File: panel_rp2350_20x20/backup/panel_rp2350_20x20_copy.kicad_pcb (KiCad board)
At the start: 6 copper layers, 45 x 45 mm, 548 parts, among them J1 Conn_01x04, J2 Conn_01x05, J3 Conn_01x05, J4 Conn_01x05, J5 Conn_01x05, SW1 SW_Push, SW2 SW_Push, U1 APS6404L-3SQR, U10 UCC27517, U11 UCC27517, U12 UCC27517, U13 UCC27517, U14 UCC27517, U15 UCC27517, U16 UCC27517, U17 UCC27517, U18 UCC27517, U19 UCC27517, U2 RP2354B_80QFN, U20 UCC27517, U21 UCC27517, U22 UCC27517, U23 UCC27517, U24 UCC27517, U25 UCC27517, U26 UCC27517, U27 UCC27517, U28 UCC27517, U29 UCC27517, U3 UCC27517, U30 UCC27517, U31 UCC27517, U32 UCC27517, U33 UCC27517, U34 UCC27517, U35 UCC27517, U36 UCC27517, U37 UCC27517, U38 UCC27517, U39 UCC27517, U4 UCC27517, U40 UCC27517, U41 UCC27517, U42 UCC27517, U43 AP2112K-3.3, U5 UCC27517, U6 UCC27517, U7 UCC27517, U8 UCC27517, U9 UCC27517, Y1 ABM8-272-T3

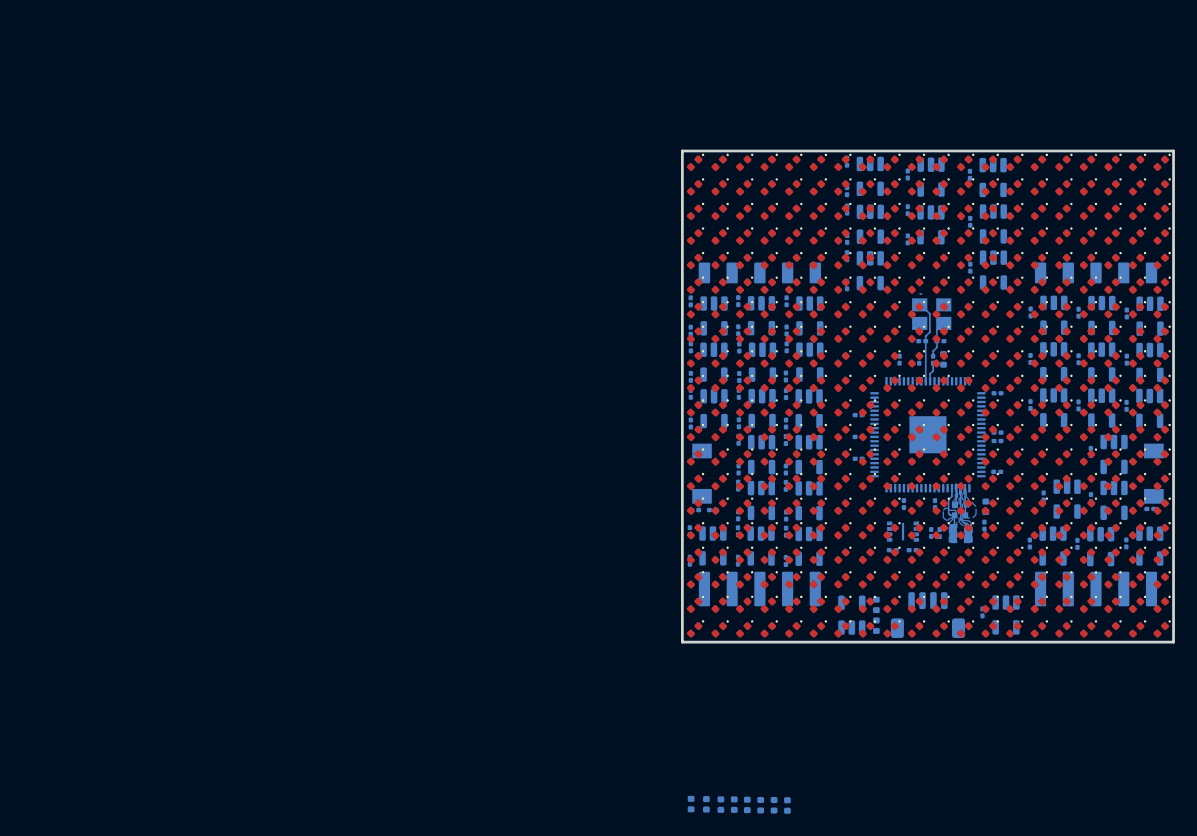
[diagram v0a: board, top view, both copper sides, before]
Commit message: More work on rp2350 20x20 panel.
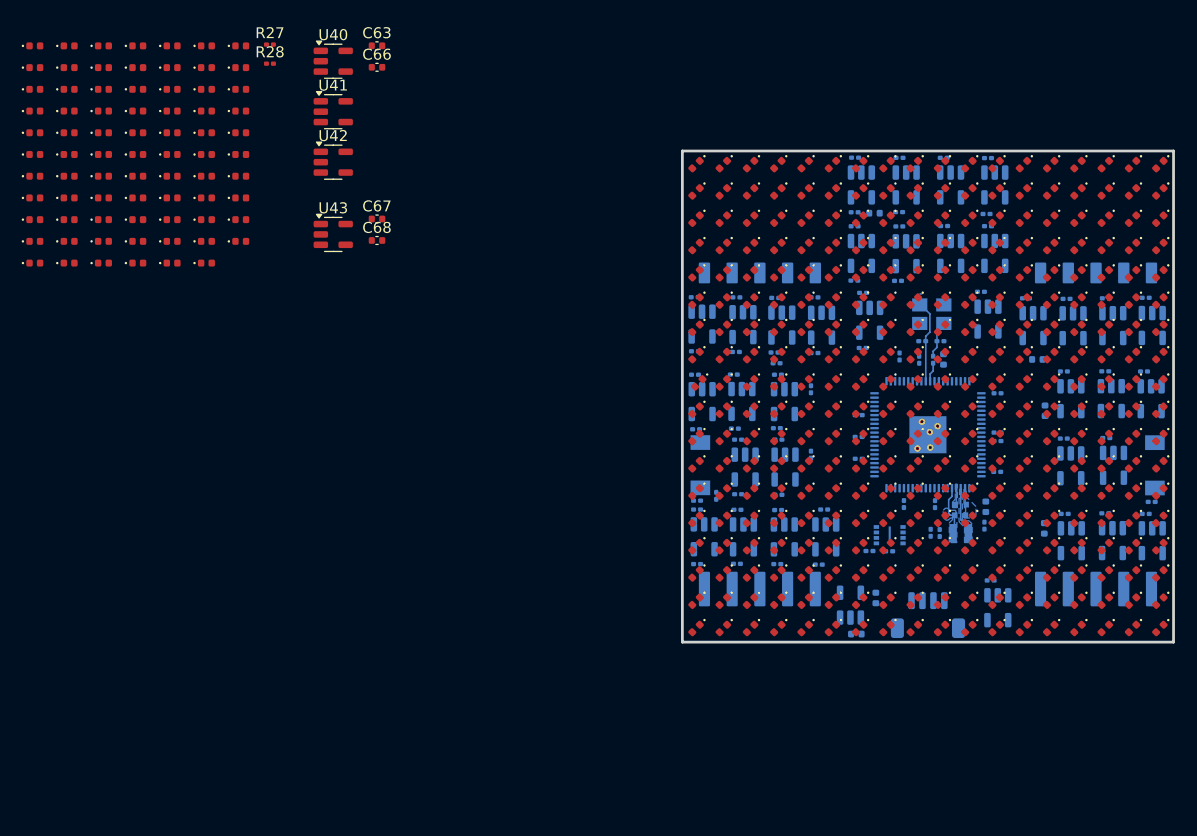
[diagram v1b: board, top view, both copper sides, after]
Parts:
- C63, C66, C67, C68, R27, R28, U40, U41, U42, U43: moved to F.Cu
- moved D331 108.3 mm to (-9.34, 52.3), turned to 0 degrees
- moved D332 106.2 mm to (-9.34, 54.3), turned to 0 degrees
- moved D351 106.2 mm to (-3.04, 48.3), turned to 0 degrees
- moved D330 104.9 mm to (-9.34, 50.3), turned to 0 degrees
- moved D333 104.3 mm to (-9.34, 56.3), turned to 0 degrees
- moved D329 104.0 mm to (-9.34, 48.3), turned to 0 degrees
- moved D352 103.7 mm to (-3.04, 50.3), turned to 0 degrees
- moved D328 103.1 mm to (-9.34, 46.3), turned to 0 degrees
- moved D350 102.9 mm to (-3.04, 46.3), turned to 0 degrees
- moved D334 102.9 mm to (-9.34, 58.3), turned to 0 degrees
- moved D327 102.2 mm to (-9.34, 44.4), turned to 0 degrees
- moved D336 102.0 mm to (-6.19, 40.4), turned to 0 degrees
- moved D335 101.8 mm to (-9.34, 60.3), turned to 0 degrees
- moved D349 101.8 mm to (-3.04, 44.4), turned to 0 degrees
- moved D353 101.6 mm to (-3.04, 52.3), turned to 0 degrees
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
